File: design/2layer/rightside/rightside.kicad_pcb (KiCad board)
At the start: 4 copper layers, 142.6 x 96.2 mm, 226 parts, among them IC2 XC9148G50CER-G, IC3 nRF52833-QDAA-R7, IC4 74AHCT125PW,118, IC5 MCP23018T-E_SS, IC6 XC9291B33D1R-G, J1 USB_C_Receptacle_USB2.0_16P, J2 Battery Pos, J3 Battery Neg, J4 OLED_128x32, J6 Conn_01x04, J7 F32Q-1A7H1-11012, U1 BQ27441-G1, U2 BQ24072RGT, U3 USB6B1, U5 PEC11L-4015F-S0015, U6 PEC11L-4015F-S0015, Y1 ECS-320-8-37B2-JTY-TR

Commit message: LS two layer complete
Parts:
- removed 5V_2, 5V_3, 5V_5, BAT_1, GND4: TestPoint, TestPoint:TestPoint_Pad_D1.5mm
- removed C20, C40, C46: 100nF, ScottoKeebs_Components:Capacitor_0603
- removed IC5: MCP23018T-E_SS, SamacSys_Parts:SOP65P780X200-24N
- removed L5: MCHK1608T1R0MKN, SamacSys_Parts:INDC1608X80N
- removed the REF** at (135.4, 38.9)
- removed the REF** at (100.9, 58.9)
- removed the REF** at (44.8, 79.6)
- removed the REF** at (82.0, 58.6)
- removed the REF** at (139.0, 76.5)
- removed the REF** at (18.2, 45.7)
- removed the REF** at (110.0, 95.7)
- removed the REF** at (80.9, 78.6)
- removed the REF** at (120.0, 58.7)
- removed the REF** at (42.4, 38.3)
- removed the REF** at (77.3, 27.9)
- removed the REF** at (63.7, 100.1)
- removed the REF** at (63.0, 105.5)
- removed the REF** at (139.1, 91.9)
- removed the REF** at (149.9, 19.0)
- removed the REF** at (18.2, 58.2)
- removed the REF** at (85.7, 109.4)
- removed the REF** at (139.0, 58.5)
- removed the REF** at (48.8, 57.5)
- removed the REF** at (106.1, 19.0)
- removed the REF** at (80.2, 92.8)
- removed the REF** at (35.5, 78.0)
- removed the REF** at (100.9, 91.9)
- removed the REF** at (135.4, 47.2)
- removed the REF** at (96.2, 38.7)
- removed the REF** at (157.1, 27.4)
- removed the REF** at (135.5, 23.1)
- removed the REF** at (49.9, 19.0)
- removed the REF** at (58.0, 38.4)
- added C47: 4.7uF, ScottoKeebs_Components:Capacitor_0603, B.Cu at (30.4, 77.5)
- added C48: 4.7uF, ScottoKeebs_Components:Capacitor_0603, B.Cu at (21.2, 23.7)
- added CHG: White LED KW_EEL, SamacSys_Parts:KWEELP41RUS1U13K6L3X4X5R18, F.Cu at (29.1, 44.6)
- added CHG1: TestPoint, TestPoint:TestPoint_Pad_D1.0mm, F.Cu at (42.3, 57.3)
- added IC1: XCL240B333FR-G, SamacSys_Parts:XCL103D503CRG, B.Cu at (29.5, 83.8)
- added IC7: SN74AHCT1G125DCKR, SamacSys_Parts:SOT65P210X110-5N, B.Cu at (27.4, 102.1)
- added LED2: White LED KW_EEL, SamacSys_Parts:KWEELP41RUS1U13K6L3X4X5R18, F.Cu at (39.9, 44.6)
- added R11: 270, Resistor_SMD:R_0603_1608Metric, F.Cu at (36.1, 44.6)
- added R12: 10k, Resistor_SMD:R_0603_1608Metric, B.Cu at (37.9, 80.3)
- added R13: 4k7, Resistor_SMD:R_0603_1608Metric, B.Cu at (43.0, 92.9)
- added R14: 4k7, Resistor_SMD:R_0603_1608Metric, B.Cu at (35.1, 86.6)
- added R15: 22, Resistor_SMD:R_0603_1608Metric, B.Cu at (28.3, 93.3)
- added R16: 22, Resistor_SMD:R_0603_1608Metric, B.Cu at (27.2, 94.3)
- added R8: 270, Resistor_SMD:R_0603_1608Metric, F.Cu at (32.9, 44.6)
- added REF**: M1.6 Hole, CustomLibrary:M1.6 Hole, F.Cu at (62.1, 98.1)
- added REF**: M1.6 Hole, CustomLibrary:M1.6 Hole, F.Cu at (64.2, 54.1)
- added REF**: M1.6 Hole, CustomLibrary:M1.6 Hole, F.Cu at (140.3, 53.8)
- added REF**: M1.6 Hole, CustomLibrary:M1.6 Hole, F.Cu at (102.2, 53.8)
- added REF**: M1.6 Hole, CustomLibrary:M1.6 Hole, F.Cu at (59.4, 34.9)
- added REF**: M1.6 Hole, CustomLibrary:M1.6 Hole, F.Cu at (19.5, 57.6)
- added REF**: M1.6 Hole, CustomLibrary:M1.6 Hole, F.Cu at (19.5, 74.5)
- added REF**: M1.6 Hole, CustomLibrary:M1.6 Hole, F.Cu at (106.4, 15.3)
- added REF**: M1.6 Hole, CustomLibrary:M1.6 Hole, F.Cu at (121.3, 73.1)
- added REF**: M1.6 Hole, CustomLibrary:M1.6 Hole, F.Cu at (43.0, 34.8)
- added REF**: M1.6 Hole, CustomLibrary:M1.6 Hole, F.Cu at (97.5, 34.5)
- added REF**: M1.6 Hole, CustomLibrary:M1.6 Hole, F.Cu at (91.9, 101.0)
- added REF**: M1.6 Hole, CustomLibrary:M1.6 Hole, F.Cu at (158.3, 21.9)
- added REF**: M1.6 Hole, CustomLibrary:M1.6 Hole, F.Cu at (81.4, 75.3)
- added ~{PGOOD}: TestPoint, TestPoint:TestPoint_Pad_D1.0mm, F.Cu at (41.1, 47.2)
- C10: value 4.7uF -> 100pF; moved to B.Cu
- C13: value 4.7uF -> 10uF
- C18: value 1uF -> 100nF
- C23, C29, C30, C34, C38, C45, C9: moved to F.Cu
- C25, C26, C27, C35, C36, C42, C44, R10: moved to B.Cu
- IC4: value 74AHCT125PW,118 -> TCA9537DGSR; footprint SamacSys_Parts:SOP65P640X110-14N -> SamacSys_Parts:SOP50P490X110-10N
- IC6: value XC9291B33D1R-G -> TPS22917LDBVT; footprint SamacSys_Parts:XC9290A07E1RG -> SamacSys_Parts:SOT95P280X145-6N
- J2: value Battery Pos -> Battery+
- J3: value Battery Neg -> Battery-
- L3: value 1uH -> 4.7uH; footprint Inductor_SMD:L_0603_1608Metric -> SamacSys_Parts:1286ASH1R0MP2
- R3: value 3k -> 540
- R4: value 1k8 -> 590
- moved REF** 141.7 mm to (144.9, 15.4)
- moved GND2 129.5 mm to (159.1, 45.6)
- moved C39 114.4 mm to (133.6, 90.9), turned to 0 degrees
- moved C43 111.5 mm to (27.5, 24.2), turned to -90 degrees
- moved C34 100.4 mm to (137.0, 18.5), turned to 0 degrees
- moved REF** 98.1 mm to (49.3, 109.8)
- moved J3 94.8 mm to (24.3, 45.1)
- moved C41 91.9 mm to (22.6, 65.4), turned to -90 degrees
- moved C17 89.5 mm to (24.6, 41.0)
- moved J2 87.9 mm to (21.5, 40.0)
- moved GND1 83.0 mm to (89.2, 97.0)
- moved C44 83.0 mm to (48.3, 32.6), turned to 180 degrees
- moved C21 80.0 mm to (85.3, 33.3), turned to -90 degrees
- moved 5V_1 73.7 mm to (136.3, 38.5)
- moved R10 69.5 mm to (25.1, 99.3), turned to 0 degrees
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- renumbered D43 to D1, D7 to D10, D9 to D11, D11 to D12, D12 to D15, D10 to D16, D8 to D17, D6 to D18, D4 to D19, D44 to D2, D2 to D20, D20 to D22, D19 to D23, D18 to D24, D17 to D25, D16 to D26, D15 to D27, D27 to D29, D45 to D3, D26 to D30, D25 to D31, D24 to D32, D23 to D33, D22 to D34, D40 to D35, D34 to D37, D32 to D38, D30 to D39, D46 to D4, D29 to D40, D31 to D41, D33 to D42, D35 to D43, D37 to D44, D38 to D45, D39 to D46, D41 to D47, D42 to D48, D47 to D5, D48 to D6, D1 to D7, D3 to D8, D5 to D9, S26 to S25, U6 to U5, U5 to U6
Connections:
- C10 pad 1: Net-(IC2-BAT) -> /OUT
- C10 pad 2: GND -> Net-(IC6-CT)
- C13 pad 1: GND -> 3V3
- C13 pad 2: 3V3 -> GND
- C17 pad 1: /BAT -> /SRP
- C18 pad 1: /BAT -> 3V3
- C25 pad 1: Net-(IC2-BAT) -> GND
- C25 pad 2: GND -> Net-(IC2-BAT)
- D1 pad 4: Net-(D42-DOUT) -> Net-(D1-DIN)
- D10 pad 2: Net-(D7-DOUT) -> Net-(D10-DOUT)
- D10 pad 4: Net-(D6-DOUT) -> Net-(D10-DIN)
- D11 pad 2: Net-(D10-DIN) -> Net-(D11-DOUT)
- D11 pad 4: Net-(D8-DOUT) -> Net-(D10-DOUT)
- D12 pad 2: Net-(D11-DOUT) -> Net-(D12-DOUT)
- D12 pad 4: Net-(D10-DOUT) -> Net-(D11-DOUT)
- D15 pad 2: Net-(D12-DOUT) -> Net-(D15-DOUT)
- D15 pad 4: Net-(D11-DOUT) -> Net-(D14-DOUT)
- D16 pad 2: Net-(D10-DOUT) -> Net-(D16-DOUT)
- D16 pad 4: Net-(D10-DIN) -> Net-(D15-DOUT)
- D17 pad 2: Net-(D8-DOUT) -> Net-(D17-DOUT)
- D17 pad 4: Net-(D7-DOUT) -> Net-(D16-DOUT)
- D18 pad 2: Net-(D6-DOUT) -> Net-(D18-DOUT)
- D18 pad 4: Net-(D5-DOUT) (its old number) -> Net-(D17-DOUT)
- D19 pad 2: Net-(D4-DOUT) (its old number) -> Net-(D19-DOUT)
- D19 pad 4: Net-(D3-DOUT) (its old number) -> Net-(D18-DOUT)
- D20 pad 2: Net-(D2-DOUT) (its old number) -> Net-(D20-DOUT)
- D20 pad 4: Net-(D1-DOUT) (its old number) -> Net-(D19-DOUT)
- D22 pad 2: Net-(D20-DOUT) -> Net-(D22-DOUT)
- D22 pad 4: Net-(D19-DOUT) -> Net-(D21-DOUT)
- D23 pad 2: Net-(D19-DOUT) -> Net-(D23-DOUT)
- D23 pad 4: Net-(D18-DOUT) -> Net-(D22-DOUT)
- D24 pad 2: Net-(D18-DOUT) -> Net-(D24-DOUT)
- D24 pad 4: Net-(D17-DOUT) -> Net-(D23-DOUT)
- D25 pad 2: Net-(D17-DOUT) -> Net-(D25-DOUT)
- D25 pad 4: Net-(D16-DOUT) -> Net-(D24-DOUT)
- D26 pad 2: Net-(D16-DOUT) -> Net-(D26-DOUT)
- D26 pad 4: Net-(D15-DOUT) -> Net-(D25-DOUT)
- D27 pad 2: Net-(D15-DOUT) -> Net-(D27-DOUT)
- D27 pad 4: Net-(D14-DOUT) -> Net-(D26-DOUT)
- D29 pad 2: Net-(D27-DOUT) -> Net-(D29-DOUT)
- D29 pad 4: Net-(D26-DOUT) -> Net-(D28-DOUT)
- D30 pad 2: Net-(D26-DOUT) -> Net-(D30-DOUT)
- D30 pad 4: Net-(D25-DOUT) -> Net-(D29-DOUT)
- D31 pad 2: Net-(D25-DOUT) -> Net-(D31-DOUT)
- D31 pad 4: Net-(D24-DOUT) -> Net-(D30-DOUT)
- D32 pad 2: Net-(D24-DOUT) -> Net-(D32-DOUT)
- D32 pad 4: Net-(D23-DOUT) -> Net-(D31-DOUT)
- D33 pad 2: Net-(D23-DOUT) -> Net-(D33-DOUT)
- D33 pad 4: Net-(D22-DOUT) -> Net-(D32-DOUT)
- D34 pad 2: Net-(D22-DOUT) -> Net-(D34-DOUT)
- D34 pad 4: Net-(D21-DOUT) -> Net-(D33-DOUT)
- D35 pad 2: Net-(D40-DOUT) -> Net-(D35-DOUT)
- D35 pad 4: Net-(D39-DOUT) -> Net-(D34-DOUT)
- D37 pad 2: Net-(D34-DOUT) -> Net-(D37-DOUT)
- D37 pad 4: Net-(D33-DOUT) -> Net-(D36-DOUT)
- D38 pad 2: Net-(D32-DOUT) -> Net-(D38-DOUT)
- D38 pad 4: Net-(D31-DOUT) -> Net-(D37-DOUT)
- D39 pad 2: Net-(D30-DOUT) -> Net-(D39-DOUT)
- D39 pad 4: Net-(D29-DOUT) -> Net-(D38-DOUT)
- D40 pad 2: Net-(D29-DOUT) -> Net-(D40-DOUT)
- D40 pad 4: Net-(D28-DOUT) -> Net-(D39-DOUT)
- D41 pad 2: Net-(D31-DOUT) -> Net-(D41-DOUT)
- D41 pad 4: Net-(D30-DOUT) -> Net-(D40-DOUT)
- D42 pad 2: Net-(D33-DOUT) -> Net-(D42-DOUT)
- D42 pad 4: Net-(D32-DOUT) -> Net-(D41-DOUT)
- D43 pad 2: Net-(D35-DOUT) -> Net-(D43-DOUT)
- D43 pad 4: Net-(D34-DOUT) -> Net-(D42-DOUT)
- D44 pad 4: Net-(D36-DOUT) -> Net-(D43-DOUT)
- D46 pad 2: Net-(D39-DOUT) -> Net-(D46-DOUT)
- D47 pad 4: Net-(D40-DOUT) -> Net-(D46-DOUT)
- D48 pad 2: Net-(D42-DOUT) -> unconnected-(D48-DOUT-Pad2)
- D6 pad 2: unconnected-(D48-DOUT-Pad2) -> Net-(D6-DOUT)
- D7 pad 2: Net-(D1-DOUT) (its old number) -> Net-(D7-DOUT)
- D7 pad 4: Net-(D1-DIN) -> Net-(D6-DOUT)
- D8 pad 2: Net-(D3-DOUT) (its old number) -> Net-(D8-DOUT)
- D8 pad 4: Net-(D2-DOUT) (its old number) -> Net-(D7-DOUT)
- D9 pad 2: Net-(D5-DOUT) (its old number) -> Net-(D10-DIN)
- D9 pad 4: Net-(D4-DOUT) (its old number) -> Net-(D8-DOUT)
- IC3 pad 12: D- -> /D2_N
- IC3 pad 13: D+ -> /D2_P
- IC3 pad 14: /CW -> /CCW2
- IC3 pad 15: /CCW -> /CW2
- IC3 pad 16: /CCW2 -> /CCW
- IC3 pad 17: /CW2 -> /CW
- IC3 pad 23: /2A -> /A
- IC3 pad 4: /Row 0 -> /Row 3
- IC3 pad 5: /Row 1 -> /Row 2
- IC3 pad 6: /Row 2 -> /Row 1
- IC3 pad 7: /Row 3 -> /Row 0
- IC4 pad 1: GND -> /NO2
- IC4 pad 10: GND -> 3V3
- IC4 pad 2: GND -> /CHG
- IC4 pad 3: unconnected-(IC4-1Y-Pad3) -> /NO
- IC4 pad 4: GND -> /GPOUT
- IC4 pad 5: /2A -> GND
- IC4 pad 6: Net-(IC4-2Y) -> Net-(IC4-~{RESET})
- IC4 pad 7: GND -> /INTA
- IC4 pad 8: unconnected-(IC4-3Y-Pad8) -> /SCL
- IC4 pad 9: GND -> /SDA
- IC6 pad 1: 3V3 -> /OUT
- IC6 pad 2: unconnected-(IC6-NC-Pad2) -> GND
- IC6 pad 3: Net-(IC2-BAT) -> Net-(IC6-ON)
- IC6 pad 4: Net-(IC2-BAT) -> Net-(IC6-CT)
- IC6 pad 5: Net-(IC6-LX) -> Net-(IC2-BAT)
- IC6 pad 6: GND -> Net-(IC2-BAT)
- J2 pad 1: /BAT -> /SRP
- L3 pad 1: 3V3 -> Net-(IC2-BAT)
- L3 pad 2: Net-(IC6-LX) -> Net-(IC2-LX)
- R10 pad 1: Net-(IC4-2Y) -> Net-(IC7-Y)
- R6 pad 2: /BAT_SRN -> /SRP
- R9 pad 1: Net-(IC5-~{RESET}) -> 3V3
- R9 pad 2: 3V3 -> Net-(IC4-~{RESET})
- S25 pad 1: Net-(IC2-BAT) -> /OUT
- S25 pad 2: /OUT -> Net-(IC6-ON)
- U1 pad 7: /BAT_SRN -> /BAT
- U1 pad 8: /BAT -> /SRP
- U2 pad 2: /BAT_SRN -> /BAT
- U2 pad 3: /BAT_SRN -> /BAT
- U2 pad 5: GND -> /BAT
- U2 pad 6: /VBUS -> GND
- U2 pad 7: unconnected-(U2-~{PGOOD}-Pad7) -> /~{PGOOD}
- U5 pad 2: /NO2 -> /NO
- U5 pad A1: /CCW2 -> /CCW
- U5 pad C1: /CW2 -> /CW
- U6 pad 2: /NO -> /NO2
- U6 pad A1: /CCW -> /CCW2
- U6 pad C1: /CW -> /CW2
- U6 pad MH1: unconnected-(U5-PadMH1) -> GND
- U6 pad MH2: unconnected-(U5-PadMH2) -> GND
- Y1 pad 1: Net-(IC3-XC2) -> Net-(IC3-XC1)
- Y1 pad 3: Net-(IC3-XC1) -> Net-(IC3-XC2)
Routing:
- net GND: track 340.5 -> 0.00 mm, vias 99 -> 0
- net /Row 0: track 217.5 -> 0.00 mm, vias 2 -> 0
- net /Column 5: track 214.1 -> 0.00 mm, vias 1 -> 0
- net /Row 1: track 200.1 -> 0.00 mm, vias 2 -> 0
- net /Column 4: track 195.5 -> 0.00 mm, vias 1 -> 0
- net /Column 3: track 178.0 -> 0.00 mm, vias 1 -> 0
- net /Row 2: track 174.1 -> 0.00 mm, vias 2 -> 0
- net /Row 3: track 172.4 -> 0.00 mm, vias 2 -> 0
- net 5V: track 169.9 -> 0.00 mm, vias 58 -> 0
- net /Column 1: track 158.5 -> 0.00 mm, vias 1 -> 0
- net /Column 2: track 157.7 -> 0.00 mm, vias 1 -> 0
- net /SCL: track 122.4 -> 0.00 mm, vias 5 -> 0
- net /SDA: track 115.5 -> 0.00 mm, vias 5 -> 0
- net /Column 0: track 108.8 -> 0.00 mm, vias 1 -> 0
- net 3V3: track 98.7 -> 0.00 mm, vias 15 -> 0
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- added copper zone on B.Cu, net 5V
- removed copper zone on In1.Cu, net /BAT
- removed copper zone on In1.Cu, net /VBUS
- removed copper zone on In1.Cu, net 3V3
- removed copper zone on In1.Cu, net 5V
- removed copper zone on B.Cu, net GND
- removed copper zone on In2.Cu, net GND
- removed copper zone on B.Cu, net Net-(IC3-ANT)
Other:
- outline, holes or cut-outs redrawn
- copper layers 4 -> 2
- board text added: "Shaheen. A 2025 Mechanical Keyboard v2.0 (hope it works :D)"
- board text removed: "Shaheen. A 2024 Mechanical Keyboard v1.0 First PCB :D"

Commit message: place components for RS 2 layer
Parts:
- removed IC2: XC9148G50CER-G, SamacSys_Parts:XC9147_8_USP-6C
- removed L3: 4.7uH, SamacSys_Parts:1286ASH1R0MP2
- added IC5: XCL110A503KR-G, SamacSys_Parts:XCL103D503CRG, B.Cu at (21.0, 27.1)
- added LED1: White LED KW_EEL, SamacSys_Parts:KWEELP41RUS1U13K6L3X4X5R18, F.Cu at (2.20, 1.45)
- added ~{PGOOD}1: TestPoint, TestPoint:TestPoint_Pad_D1.0mm, F.Cu at (1.02, 4.92)
- C26: value 10uF-lowESR -> 10uF
- F1: value 600mA -> 6A
- moved IC4 36.3 mm to (3.18, 90.8)
- moved C2 16.3 mm to (12.9, 88.6)
- moved R15 15.7 mm to (13.6, 98.8)
- moved R16 15.7 mm to (12.5, 99.8)
- moved Y1 15.3 mm to (24.2, 101.6), turned to 180 degrees
- moved REF** 13.2 mm to (61.4, 114.9)
- moved C14 12.5 mm to (24.8, 98.9), turned to 0 degrees
- moved C26 12.3 mm to (16.4, 29.8)
- moved C25 10.4 mm to (22.5, 31.1)
- moved R9 9.65 mm to (46.1, 96.0)
- moved C1 9.00 mm to (39.5, 94.8)
- moved C11 8.37 mm to (36.6, 99.8)
- moved C7 8.29 mm to (14.1, 92.4)
- moved R5 8.18 mm to (28.1, 29.5), turned to 90 degrees
- moved C22 7.44 mm to (27.4, 43.5)
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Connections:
- C26 pad 1: 5V -> GND
- C26 pad 2: GND -> 5V
- IC3 pad 14: /CCW2 -> /Column 2
- IC3 pad 15: /CW2 -> /Column 3
- IC3 pad 16: /CCW -> /Column 4
- IC3 pad 17: /CW -> /Column 5
- IC3 pad 22: /INTA -> /Column 0
- IC3 pad 23: /A -> /Column 1
- IC3 pad 31: /Column 5 -> /A
- IC3 pad 32: /Column 4 -> /CW
- IC3 pad 33: /Column 3 -> /CCW
- IC3 pad 34: /Column 2 -> /CW2
- IC3 pad 35: /Column 1 -> /CCW2
- IC3 pad 36: /Column 0 -> /INTA
- IC3 pad 4: /Row 3 -> /Row 0
- IC3 pad 5: /Row 2 -> /Row 1
- IC3 pad 6: /Row 1 -> /Row 2
- IC3 pad 7: /Row 0 -> /Row 3
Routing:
- net GND: track 0.00 -> 40.2 mm, vias 0 -> 14
- net /BAT: track 0.00 -> 26.5 mm
- net /OUT: track 0.00 -> 14.5 mm
- net /SRP: track 0.00 -> 12.7 mm, vias 0 -> 2
- net /VBUS_USB: track 0.00 -> 11.1 mm
- net Net-(IC3-XC2): track 0.00 -> 9.95 mm
- net Net-(IC6-CT): track 0.00 -> 9.49 mm
- net /VBUS: track 0.00 -> 9.15 mm, vias 0 -> 1
- net /D_P: track 0.00 -> 8.94 mm
- net /D_N: track 0.00 -> 8.91 mm
- net Net-(D1-DIN): track 0.00 -> 8.28 mm, vias 0 -> 1
- net Net-(IC3-XC1): track 0.00 -> 8.13 mm
- net /A: track 0.00 -> 5.29 mm
- net Net-(IC3-DEC3): track 0.00 -> 4.98 mm
- net /Column 1: track 0.00 -> 4.25 mm
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
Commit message: prepare to add in EVQWGD001
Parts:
- removed C27: 10uF-lowESR, ScottoKeebs_Components:Capacitor_0603
- removed the REF** at (158.3, 21.9)
- added R17: 0, Resistor_SMD:R_0603_1608Metric, B.Cu at (30.4, 75.5)
- moved IC4 43.5 mm to (41.2, 69.6)
- moved C1 33.7 mm to (5.78, 94.1)
- moved C8 33.7 mm to (7.28, 97.5)
- moved C13 28.7 mm to (7.68, 84.3)
- moved C18 26.5 mm to (15.5, 85.5)
- moved R9 25.8 mm to (43.8, 70.3), turned to -90 degrees
- moved R16 25.7 mm to (37.7, 94.5)
- moved R15 23.6 mm to (36.6, 93.4)
- moved C2 20.8 mm to (33.4, 85.8)
- moved C5 19.5 mm to (15.7, 88.9)
- moved R12 18.1 mm to (43.0, 62.9), turned to 180 degrees
- moved C43 13.4 mm to (14.1, 25.3)
- moved C47 12.6 mm to (17.8, 77.9)
- moved J7 12.0 mm to (27.1, 79.4)
- moved R13 10.6 mm to (33.3, 88.6), turned to 0 degrees
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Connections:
- C2 pad 2: /VBUS -> Net-(IC3-VBUS)
- IC3 pad 10: /VBUS -> Net-(IC3-VBUS)
- IC3 pad 2: /SCL -> /Row 0
- IC3 pad 3: /SDA -> /Row 1
- IC3 pad 32: /CW -> /CCW
- IC3 pad 33: /CCW -> /CW
- IC3 pad 34: /CW2 -> /CCW2
- IC3 pad 35: /CCW2 -> /CW2
- IC3 pad 4: /Row 0 -> /Row 2
- IC3 pad 5: /Row 1 -> /Row 3
- IC3 pad 6: /Row 2 -> /SCL
- IC3 pad 7: /Row 3 -> /SDA
- IC4 pad 1: /NO2 -> /CHG
- IC4 pad 2: /CHG -> /NO2
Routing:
- net 5V: track 0.00 -> 92.5 mm, vias 0 -> 11
- net D+: track 0.00 -> 72.8 mm
- net D-: track 0.00 -> 71.9 mm
- net /CCW: track 0.00 -> 64.4 mm
- net /CW: track 0.00 -> 63.0 mm
- net /VBUS: track 9.15 -> 64.1 mm
- net /GPOUT: track 0.00 -> 45.5 mm, vias 0 -> 4
- net /NO: track 0.00 -> 44.0 mm
- net /CW2: track 0.00 -> 41.7 mm
- net /CCW2: track 0.00 -> 41.2 mm
- net /INTA: track 0.00 -> 35.6 mm, vias 0 -> 2
- net 3V3: track 0.00 -> 31.1 mm, vias 0 -> 1
- net /CHG: track 0.00 -> 29.4 mm, vias 0 -> 5
- net Net-(D5-DOUT): track 0.00 -> 23.9 mm, vias 0 -> 4
- net Net-(IC5-1/VIN): track 0.65 -> 23.1 mm, vias 1 -> 0
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
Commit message: New layout
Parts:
- removed St1: Stabilizer_MX_2.00u, ScottoKeebs_Stabilizer:Stabilizer_MX_2.00u
- removed U6: PEC11L-4015F-S0015, SamacSys_Parts:PEC11L4015FS0015
- added EVQWGD1: ~, SamacSys_Parts:RollerEncoder_Panasonic_EVQWGD001, F.Cu at (34.6, 80.8)
- Di15: moved to F.Cu
- IC1, IC5: footprint SamacSys_Parts:XCL103D503CRG -> SamacSys:XCL103D503CRG
- IC4: footprint SamacSys_Parts:SOP50P490X110-10N -> SamacSys:SOP50P490X110-10N
- IC6: footprint SamacSys_Parts:SOT95P280X145-6N -> SamacSys:SOT95P280X145-6N
- IC7: footprint SamacSys_Parts:SOT65P210X110-5N -> SamacSys:SOT65P210X110-5N
- J7: footprint SamacSys_Parts:F32Q1A7H111012 -> SamacSys:F32Q1A7H111012
- LED1, LED2: footprint SamacSys_Parts:KWEELP41RUS1U13K6L3X4X5R18 -> SamacSys:KWEELP41RUS1U13K6L3X4X5R18
- R6: footprint SamacSys_Parts:RESC2012X41N -> SamacSys:RESC2012X41N
- Y1: footprint SamacSys_Parts:ECS320837B2JTYTR -> SamacSys:ECS320837B2JTYTR
- moved Di15 156.6 mm to (2.38, 18.4), turned to 0 degrees
- moved D26 117.1 mm to (30.8, 58.5), turned to 0 degrees
- moved S12 117.1 mm to (30.8, 53.8)
- moved S25 102.6 mm to (68.7, 110.9), turned to 0 degrees
- moved C17 49.6 mm to (-25.0, 43.0)
- moved C22 49.6 mm to (-22.2, 45.6)
- moved CHG 49.6 mm to (-20.5, 46.7)
- moved LED2 49.6 mm to (-9.68, 46.6)
- moved R11 49.6 mm to (-13.5, 46.7)
- moved R8 49.6 mm to (-16.7, 46.7)
- moved J3 40.7 mm to (-9.68, 68.1)
- moved J2 38.3 mm to (-12.1, 58.6)
- moved IC4 36.8 mm to (4.61, 65.7)
- moved U3 35.4 mm to (4.13, 13.4)
- moved C24 31.2 mm to (2.23, 40.3)
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- renumbered D44 to D43, D43 to D44
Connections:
- D43 pad 2: Net-(D44-DOUT) -> Net-(D43-DOUT)
- D43 pad 4: Net-(D43-DOUT) -> Net-(D42-DOUT)
- D44 pad 2: Net-(D43-DOUT) -> Net-(D44-DOUT)
- D44 pad 4: Net-(D42-DOUT) -> Net-(D43-DOUT)
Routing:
- net 5V: track 92.5 -> 0.00 mm, vias 11 -> 0
- net D+: track 72.8 -> 0.00 mm
- net D-: track 71.9 -> 0.00 mm
- net /CCW: track 64.4 -> 0.00 mm
- net /VBUS: track 64.1 -> 0.00 mm, vias 1 -> 0
- net /CW: track 63.0 -> 0.00 mm
- net GND: track 61.2 -> 0.00 mm, vias 30 -> 0
- net /GPOUT: track 45.5 -> 0.00 mm, vias 4 -> 0
- net /NO: track 44.0 -> 0.00 mm
- net /CW2: track 41.7 -> 0.00 mm
- net /CCW2: track 41.2 -> 0.00 mm
- net /BAT: track 40.6 -> 0.00 mm, vias 1 -> 0
- net /INTA: track 35.6 -> 0.00 mm, vias 2 -> 0
- net 3V3: track 31.1 -> 0.00 mm, vias 1 -> 0
- net /CHG: track 29.4 -> 0.00 mm, vias 5 -> 0
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- removed copper zone on B.Cu, net 5V
- removed copper zone on F.Cu, net GND
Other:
- board size 142.6 x 96.2 mm -> 142.6 x 98.8 mm
- board text added: "Shaheen. A 2025 Mechanical Keyboard #2.0 (hope it works :D)"
- board text removed: "Shaheen. A 2025 Mechanical Keyboard v2.0 (hope it works :D)"

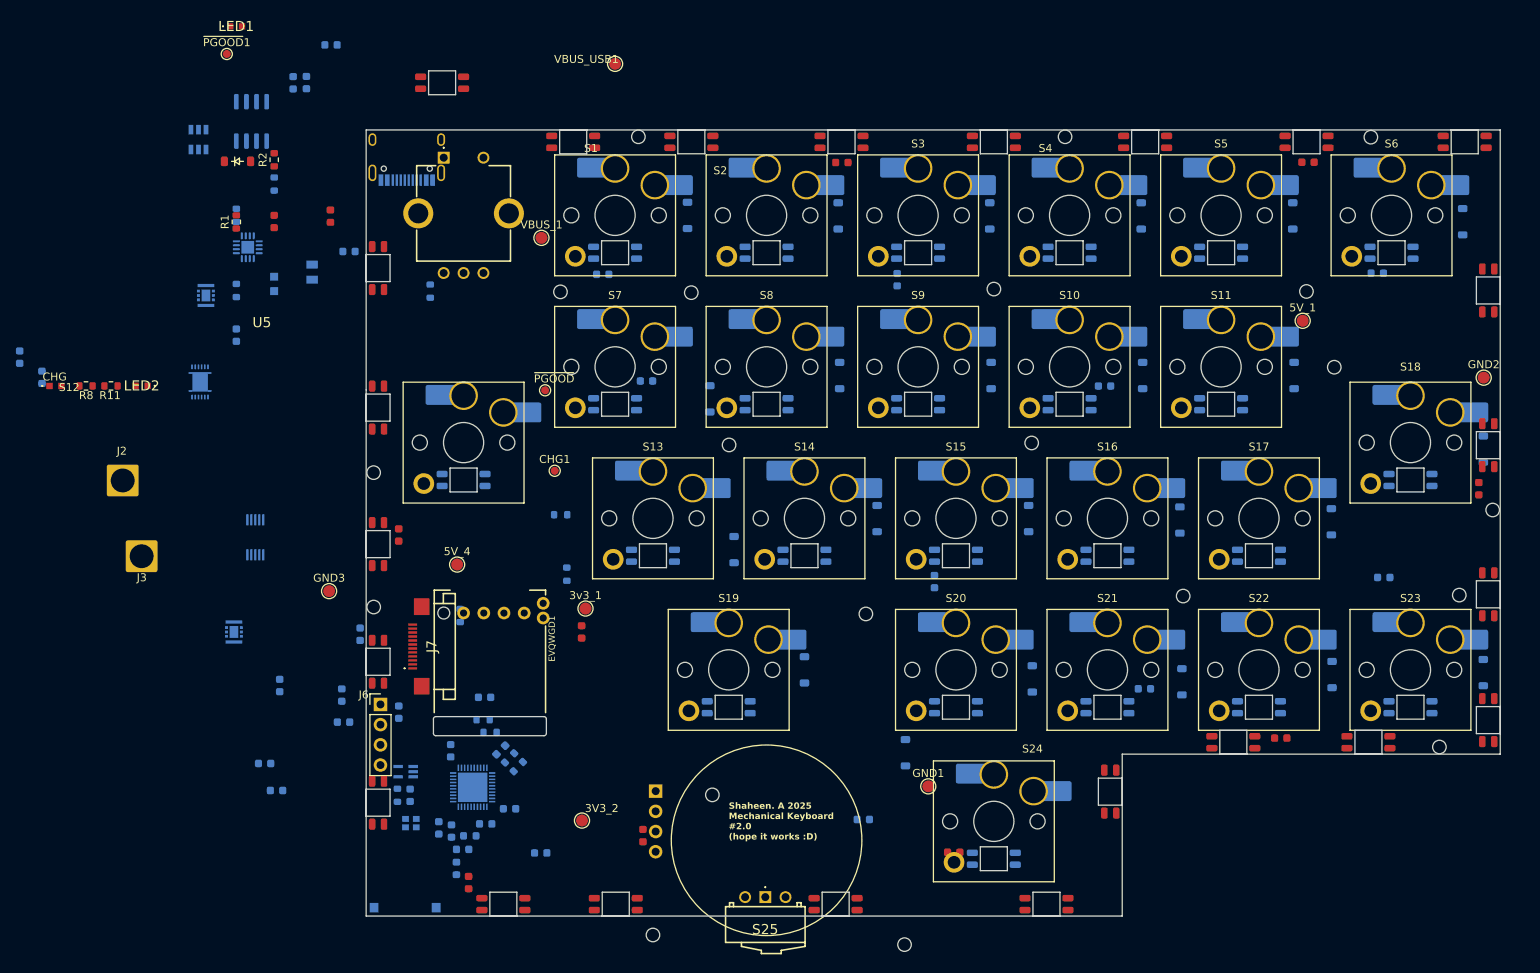
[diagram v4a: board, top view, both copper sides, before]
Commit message: RS begin to replace USB lines to shift 5V planes
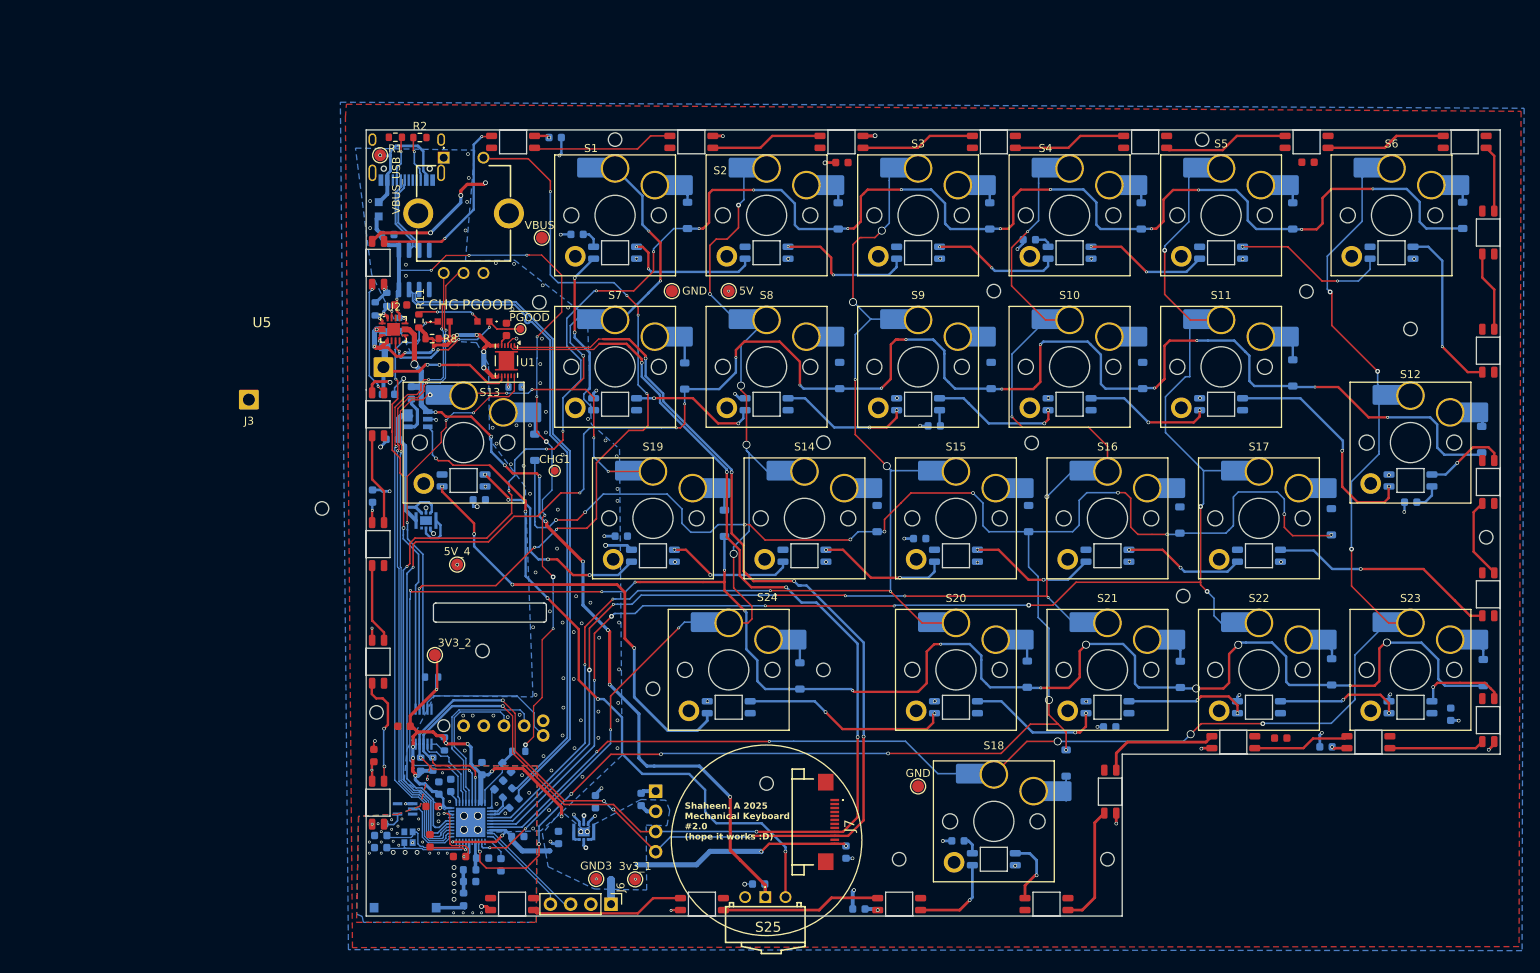
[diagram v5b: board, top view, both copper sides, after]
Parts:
- removed the CHG at (-20.5, 46.7)
- removed the REF** at (62.1, 98.1)
- removed the REF** at (160.2, 62.3)
- removed ~{PGOOD}1: TestPoint, TestPoint:TestPoint_Pad_D1.0mm
- C12, C18, C22, C32, C6, C8, D46, U1, U2: moved to F.Cu
- C29, C37, C38, C41, C43, C45, C9, D45, Di15, EVQWGD1, J2, REF**: moved to B.Cu
- moved Di15 160.3 mm to (158.8, 53.4), turned to 90 degrees
- moved D6 132.9 mm to (159.7, 27.4), turned to -90 degrees
- moved D26 119.1 mm to (149.9, 58.6)
- moved D29 119.1 mm to (30.8, 58.6), turned to 180 degrees
- moved S12 119.1 mm to (149.9, 53.8)
- moved C48 115.7 mm to (67.9, 109.3), turned to 0 degrees
- moved GND 102.7 mm to (57.0, 34.7)
- moved REF** 86.4 mm to (76.0, 53.8)
- moved C43 84.5 mm to (88.2, 65.9), turned to 180 degrees
- moved C36 75.8 mm to (42.3, 15.4), turned to 0 degrees
- moved C31 75.0 mm to (154.9, 87.9), turned to -90 degrees
- moved C32 73.8 mm to (19.5, 93.1), turned to 90 degrees
- moved 5V 72.3 mm to (64.1, 34.7)
- moved S18 70.8 mm to (97.5, 101.4)
- moved C29 68.9 mm to (90.0, 51.7), turned to 180 degrees
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- renumbered 5V_1 to 5V, LED1 to CHG, GND2 to GND, GND1 to GND, LED2 to PGOOD, VBUS_1 to VBUS, VBUS_USB1 to VBUS_USB
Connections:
- D14 pad 4: Net-(D13-DOUT) -> Net-(D14-DIN)
- D29 pad 4: Net-(D28-DOUT) -> Net-(D29-DIN)
- D30 pad 4: Net-(D29-DOUT) -> Net-(D28-DOUT)
- D34 pad 2: Net-(D34-DOUT) -> Net-(D29-DIN)
- D35 pad 4: Net-(D34-DOUT) -> Net-(D29-DOUT)
- D6 pad 2: Net-(D6-DOUT) -> Net-(D14-DIN)
- D6 pad 4: Net-(D5-DOUT) -> Net-(D13-DOUT)
- D7 pad 4: Net-(D6-DOUT) -> Net-(D5-DOUT)
- IC3 pad 2: /Row 0 -> /Row 3
- IC3 pad 22: /Column 0 -> /Column 1
- IC3 pad 23: /Column 1 -> /Row 2
- IC3 pad 3: /Row 1 -> /INTA
- IC3 pad 34: /CCW2 -> /Column 0
- IC3 pad 35: /CW2 -> /Row 0
- IC3 pad 36: /INTA -> /Row 1
- IC3 pad 4: /Row 2 -> /CW2
- IC3 pad 5: /Row 3 -> /CCW2
- IC3 pad 6: /SCL -> /SDA
- IC3 pad 7: /SDA -> /SCL
- IC4 pad 2: /NO2 -> /NO
- IC4 pad 3: /NO -> /GPOUT
- IC4 pad 4: /GPOUT -> /NO2
- R13 pad 1: /SCL -> /SDA
- R14 pad 1: /SDA -> /SCL
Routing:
- net /Row 2: track 0.00 -> 253.0 mm, vias 0 -> 17
- net /Row 0: track 0.00 -> 243.7 mm, vias 0 -> 16
- net /Row 1: track 0.00 -> 231.7 mm, vias 0 -> 14
- net /Row 3: track 0.00 -> 217.9 mm, vias 0 -> 13
- net /Column 5: track 0.00 -> 202.1 mm, vias 0 -> 8
- net /Column 4: track 0.00 -> 188.6 mm, vias 0 -> 8
- net /Column 3: track 0.00 -> 177.4 mm, vias 0 -> 9
- net /SDA: track 0.00 -> 175.7 mm, vias 0 -> 10
- net /SCL: track 0.00 -> 170.5 mm, vias 0 -> 8
- net /Column 2: track 0.00 -> 149.6 mm, vias 0 -> 8
- net /Column 0: track 0.00 -> 133.5 mm, vias 0 -> 9
- net /Column 1: track 0.00 -> 120.8 mm, vias 0 -> 9
- net 3V3: track 0.00 -> 111.5 mm, vias 0 -> 14
- net /NO: track 0.00 -> 106.1 mm, vias 0 -> 7
- net /VBUS: track 0.00 -> 102.3 mm, vias 0 -> 11
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- added copper zone on B.Cu, net 3V3
- added copper zone on B.Cu, net 5V
- added copper zone on B.Cu, net GND
- added copper zone on F.Cu, net GND
